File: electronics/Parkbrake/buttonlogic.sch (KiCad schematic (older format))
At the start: 38 parts, among them Q39 BSS308, U28 SN74HC20, U29 SN74HC02, U30 SN74HC132

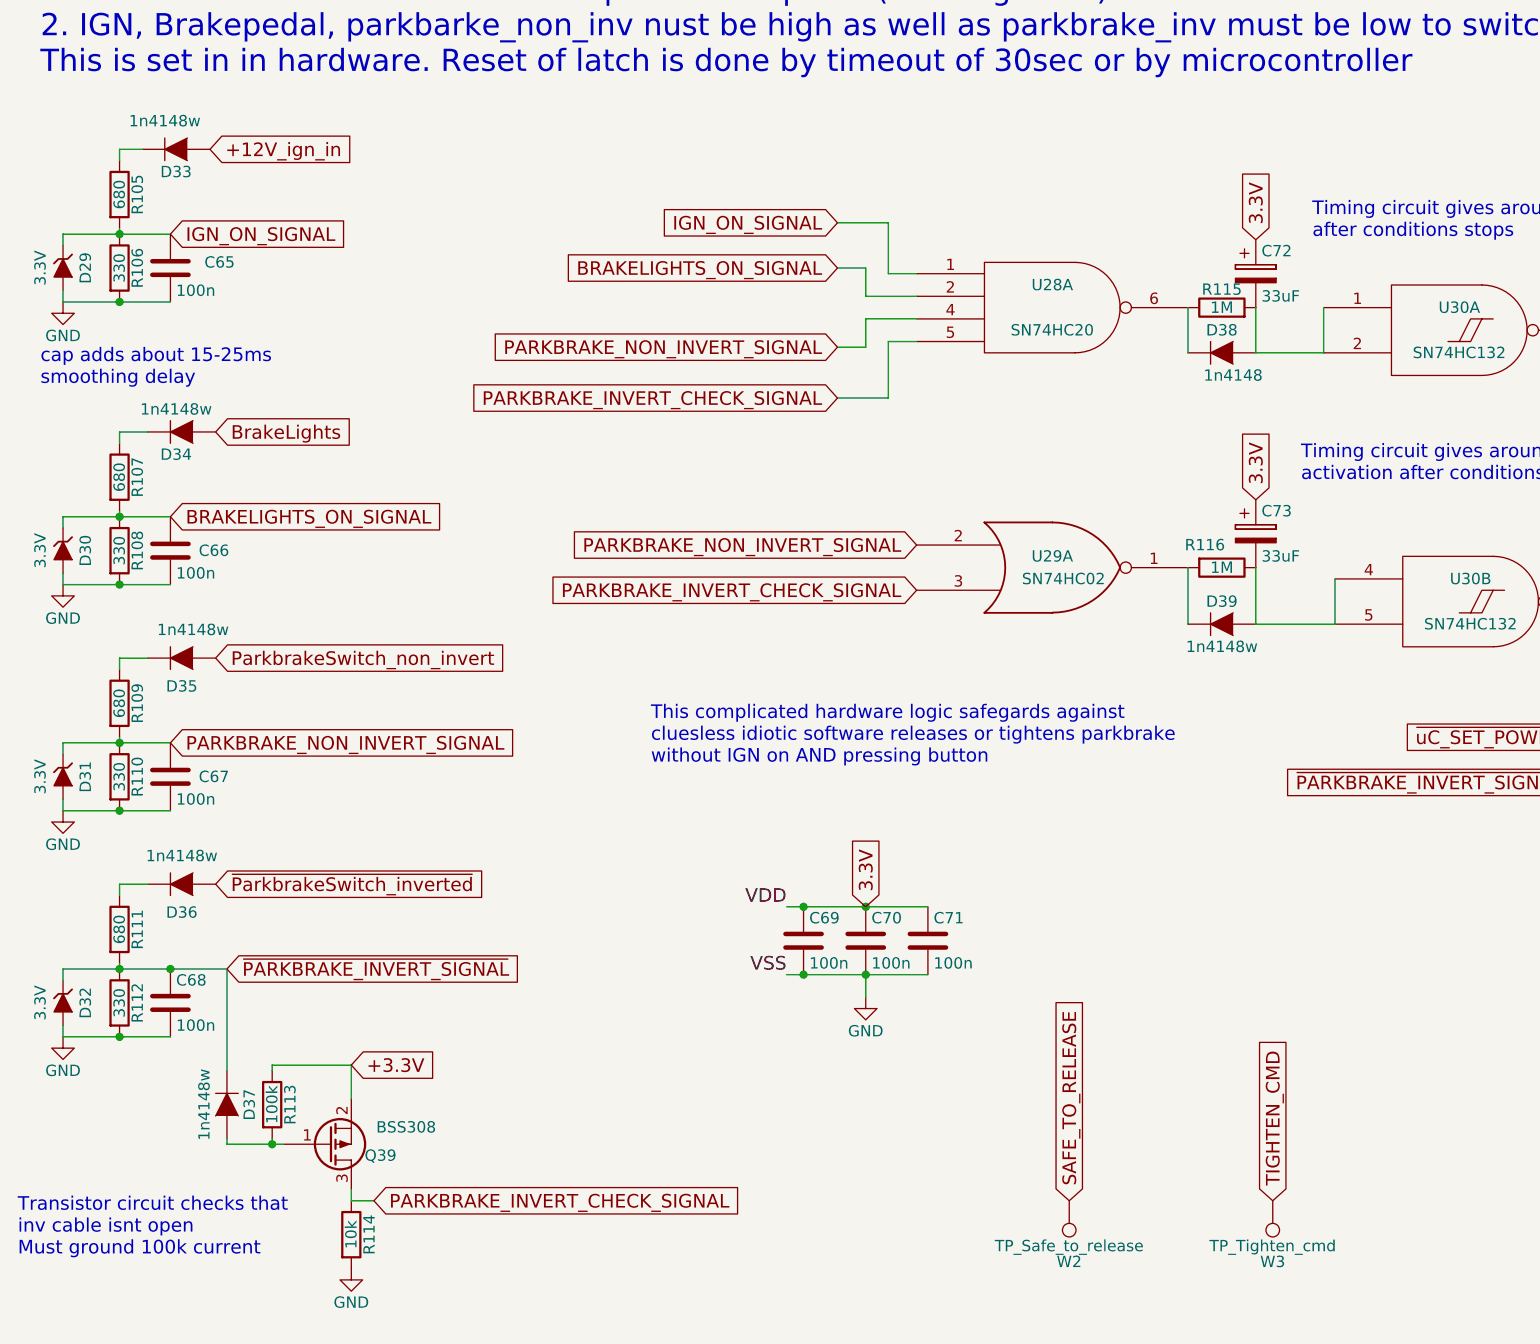
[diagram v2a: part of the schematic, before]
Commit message: More fixes and chenged components eat less boardspace
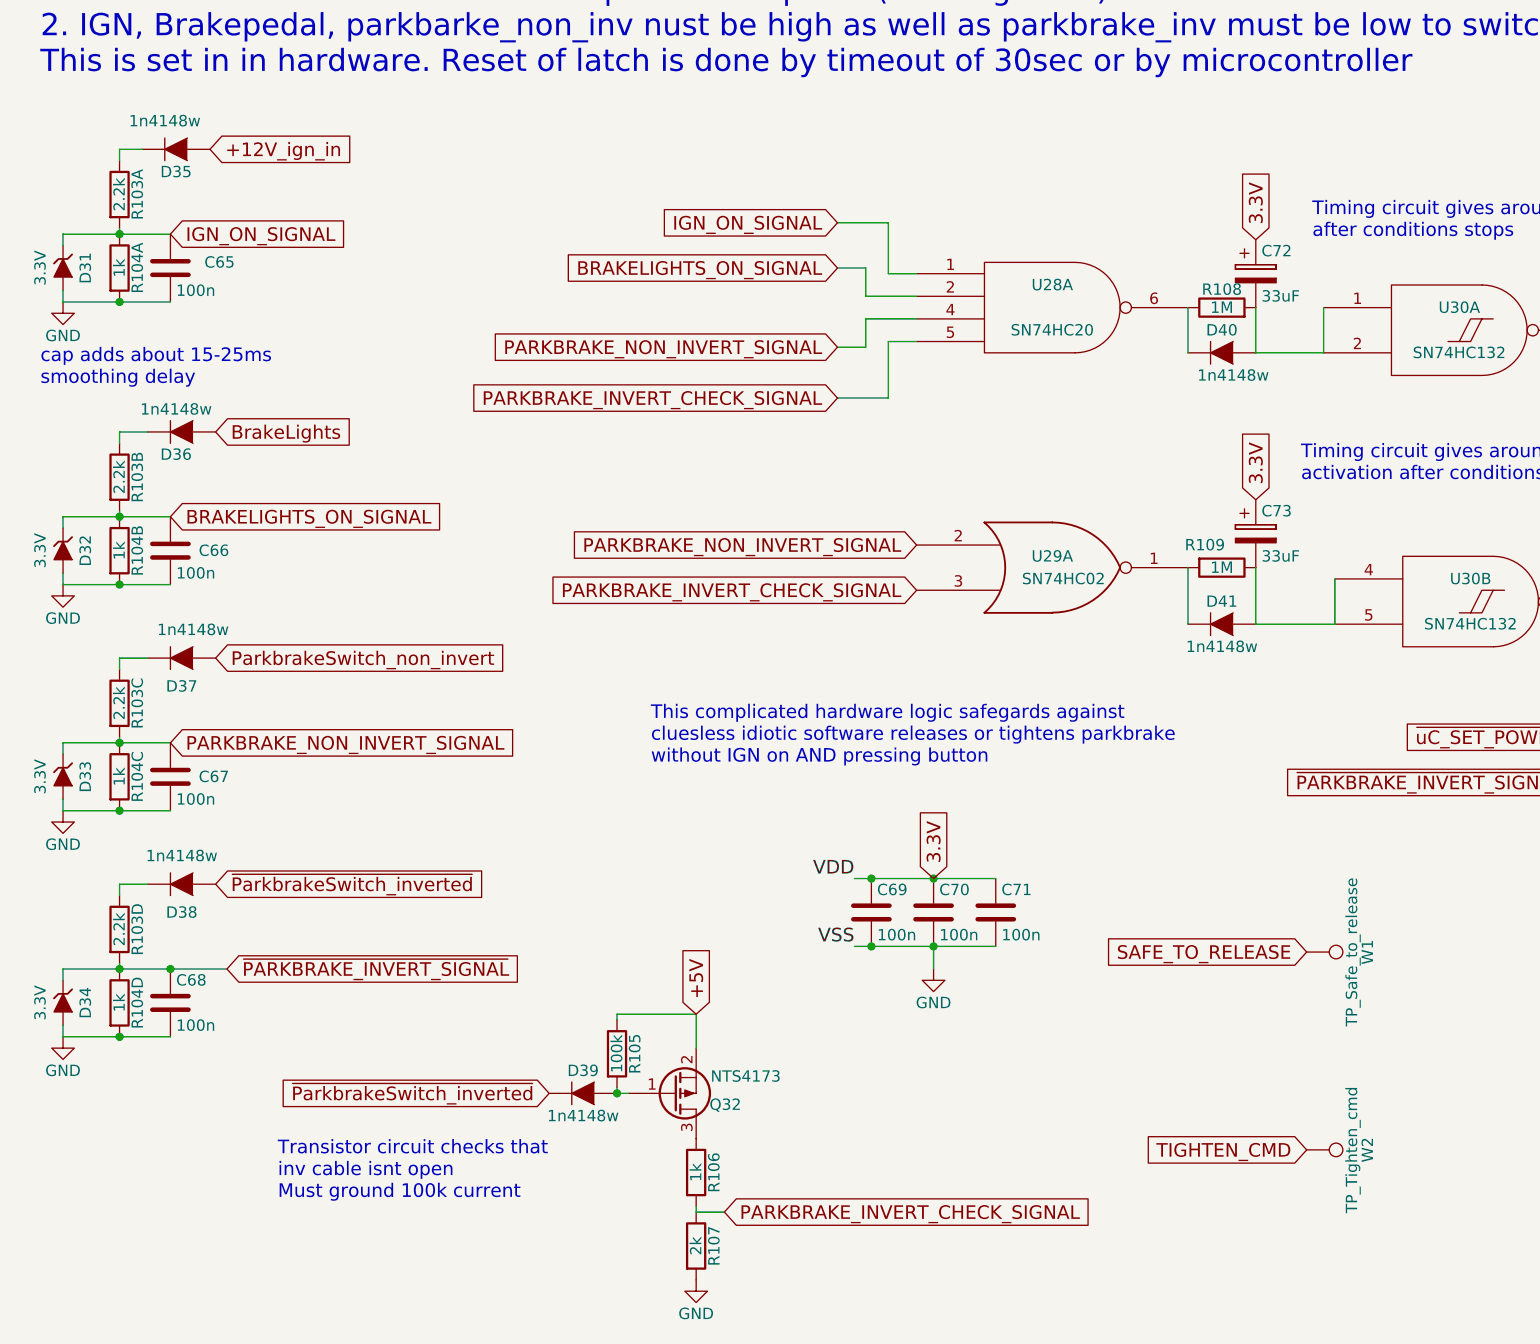
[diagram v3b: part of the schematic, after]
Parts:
- removed R105, R109, R111: 680, symbol R
- removed R106, R108, R110, R112: 330, Resistors_SMD:R_0805, symbol R
- added R103: 2.2k, symbol Rnet4
- added R104: 1k, Resistors_SMD:R_Array_Concave_4x0603, symbol Rnet4
- C72, C73: footprint Capacitors_SMD:c_elec_4x5.3 -> myfootprints:CP_1206; farnell 2069144 -> 1754149; part EXV336M6R3A9BAA -> 293D336X96R3A2TE3
- D31: renamed from D29; footprint Diodes_SMD:SOD-123 -> Diodes_SMD:SOD-323; farnell 2454044 -> 2463489; part MMSZ4684 -> MM3Z3V3ST1G
- D32: renamed from D30; footprint Diodes_SMD:SOD-123 -> Diodes_SMD:SOD-323; farnell 2454044 -> 2463489; part MMSZ4684 -> MM3Z3V3ST1G
- D33: renamed from D31; footprint Diodes_SMD:SOD-123 -> Diodes_SMD:SOD-323; farnell 2454044 -> 2463489; part MMSZ4684 -> MM3Z3V3ST1G
- D34: renamed from D32; footprint Diodes_SMD:SOD-123 -> Diodes_SMD:SOD-323; farnell 2454044 -> 2463489; part MMSZ4684 -> MM3Z3V3ST1G
- D35: renamed from D33; footprint Diodes_SMD:SOD-123 -> Diodes_SMD:SOD-323; farnell 2433353 -> 1466524; part 1N4148W-E3-08 -> 1N4148WS
- D36: renamed from D34; footprint Diodes_SMD:SOD-123 -> Diodes_SMD:SOD-323; farnell 2433353 -> 1466524; part 1N4148W-E3-08 -> 1N4148WS
- D37: renamed from D35; footprint Diodes_SMD:SOD-123 -> Diodes_SMD:SOD-323; farnell 2433353 -> 1466524; part 1N4148W-E3-08 -> 1N4148WS
- D38: renamed from D36; footprint Diodes_SMD:SOD-123 -> Diodes_SMD:SOD-323; farnell 2433353 -> 1466524; part 1N4148W-E3-08 -> 1N4148WS
- D39: renamed from D37; footprint Diodes_SMD:SOD-123 -> Diodes_SMD:SOD-323; farnell 2433353 -> 1466524; part 1N4148W-E3-08 -> 1N4148WS
- D40: renamed from D38; value 1n4148 -> 1n4148w; footprint Diodes_SMD:SOD-123 -> Diodes_SMD:SOD-323; farnell 2433353 -> 1466524; part 1N4148W-E3-08 -> 1N4148WS
- D41: renamed from D39; footprint Diodes_SMD:SOD-123 -> Diodes_SMD:SOD-323; farnell 2433353 -> 1466524; part 1N4148W-E3-08 -> 1N4148WS
- Q32: renamed from Q39; value BSS308 -> NTS4173; footprint TO_SOT_Packages_SMD:SOT-23 -> TO_SOT_Packages_SMD:SOT-323; farnell 2432719 -> 2533203; part BSS308PE H6327 -> NTS4173PT1G
- R106: renamed from R114; value 10k -> 1k; farnell 9332391 -> 9332383; part MC01W0805110K -> MC01W080511K
- R107: value 680 -> 2k; footprint (none) -> Resistors_SMD:R_0805; farnell 9333460 -> 9332766; part MC01W08051680R -> MC01W080512K
- U29, U30: footprint (none) -> Housings_SSOP:TSSOP-14_4.4x5mm_Pitch0.65mm
- U30: farnell (none) -> 2342491
- W1: renamed from W2; footprint (none) -> Measurement_Points:Measurement_Point_Round-SMD-Pad_Small
- W2: renamed from W3; footprint (none) -> Measurement_Points:Measurement_Point_Round-SMD-Pad_Small
- renumbered R113 to R105, R115 to R108, R116 to R109
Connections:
- net BRAKELIGHTS_ON_SIGNAL: now also R103.7, R104.2; no longer R107.2
- net GND: now also R107.2, R104.5, R104.6, R104.7, R104.8; no longer R106.2
- net IGN_ON_SIGNAL: now also R103.8, R104.1
- net PARKBRAKE_INVERT_CHECK_SIGNAL: now also R106.2, R107.1; no longer Q32.3 (D), R106.1
- net PARKBRAKE_NON_INVERT_SIGNAL: now also R103.6, R104.3
- net ~PARKBRAKE_INVERT_SIGNAL: now also R103.5, R104.4; no longer D39.1 (K)
- net ~ParkbrakeSwitch_inverted: now also D39.1 (K)
- net at D35.1 (K): now also R103.1
- net at D36.1 (K): now also R103.2; no longer R107.1
- net at D37.1 (K): now also R103.3
- net at D38.1 (K): now also R103.4
- net +3.3V renamed +5V
- new net: Q32.3 (D), R106.1
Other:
- moved on the sheet: C69, C70, C71, D39, Q32, R105, R106, W1, W2
